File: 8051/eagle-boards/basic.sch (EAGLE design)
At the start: 29 parts, among them IC1 AT89S51-24P, IC2 ULN2003AN, IC3 ULN2003AN, Q1 12M

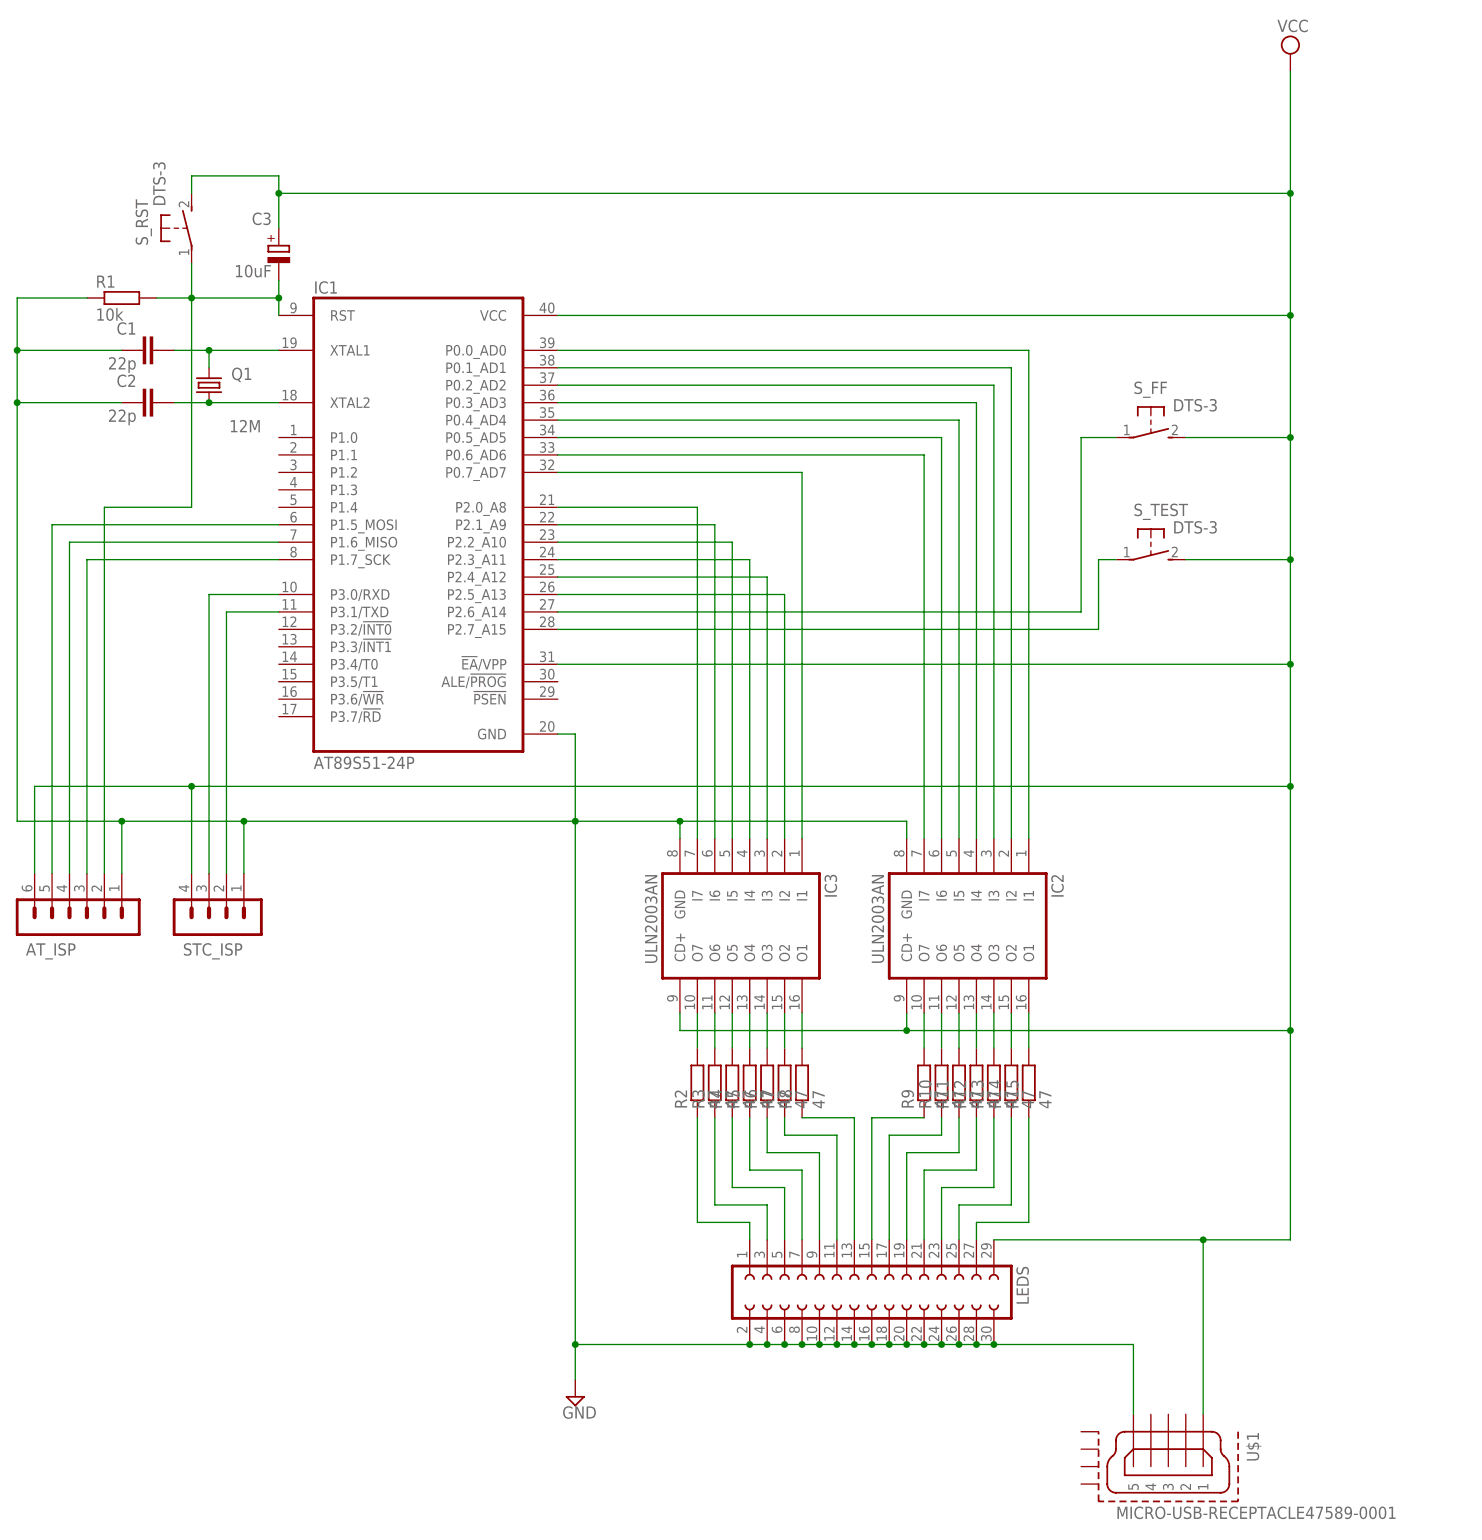
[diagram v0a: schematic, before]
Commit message: Split the actuation into its own board.
Note that the previous design was broken, as the Darlingtons weren't being grounded, but rather joined to Vcc.
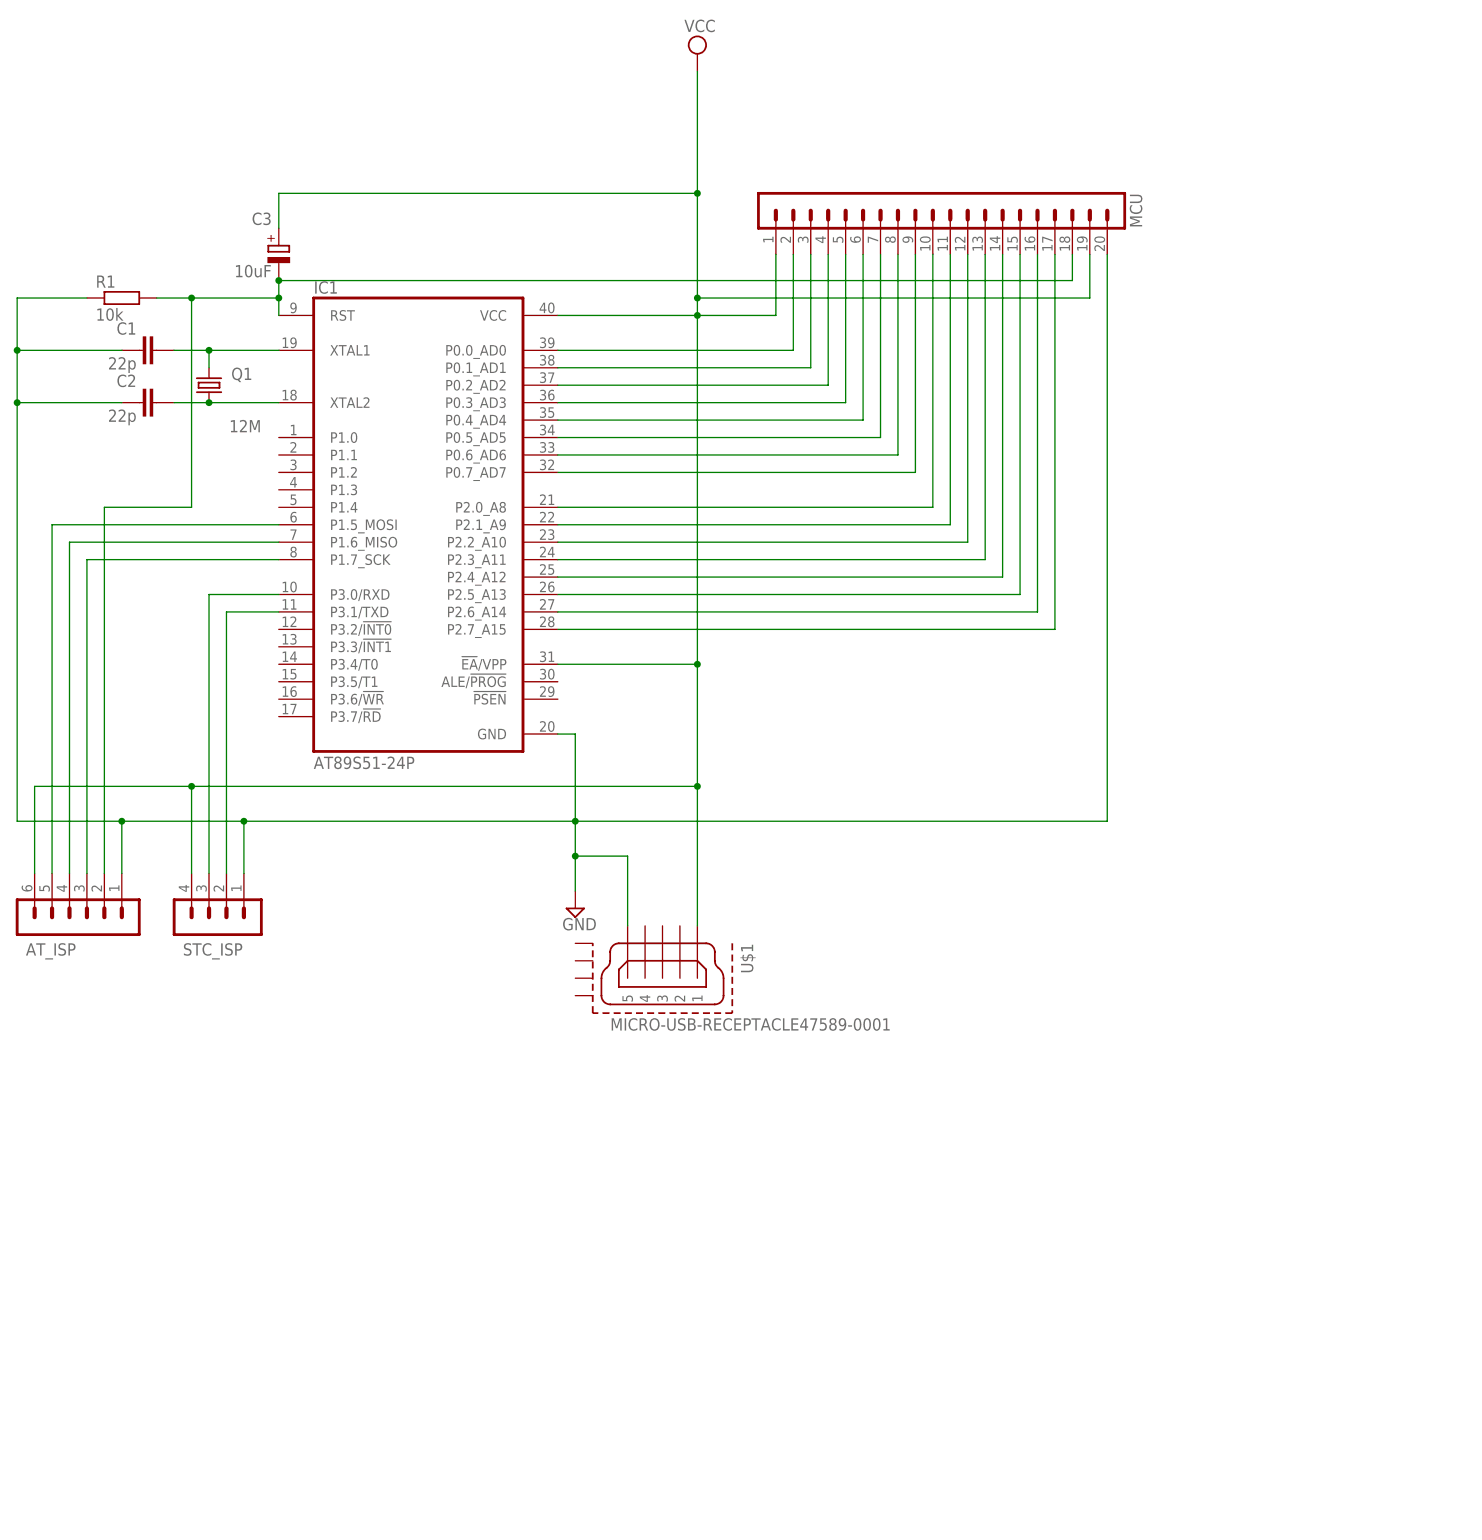
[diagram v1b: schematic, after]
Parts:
- removed IC2, IC3: ULN2003AN, uln-udn:ULN2003AN
- removed LEDS: (no value), con-lsta:FE15-2
- removed R10, R11, R12, R13, R14, R15, R2, R3, R4, R5, R6, R7, R8, R9: 47, rcl:R-EU_0207/10
- removed S_FF, S_RST, S_TEST: DTS-3, switch-tact:DTS-3
- added MCU: (no value), con-lstb:MA20-1
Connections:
- removed net N$21: IC3.O6, R3.2
- removed net N$22: IC3.O5, R4.2
- removed net N$23: IC3.O4, R5.2
- removed net N$24: IC3.O3, R6.2
- removed net N$25: IC3.O2, R7.2
- removed net N$26: IC3.O1, R8.2
- removed net N$27: IC2.O7, R9.2
- removed net N$28: IC2.O6, R10.2
- removed net N$29: IC2.O5, R11.2
- removed net N$30: IC2.O4, R12.2
- removed net N$31: IC2.O3, R13.2
- removed net N$32: IC2.O2, R14.2
- removed net N$33: IC2.O1, R15.2
- removed net N$34: LEDS.27, R15.1
- removed net N$35: LEDS.25, R14.1
- removed net N$36: LEDS.23, R13.1
- removed net N$37: LEDS.21, R12.1
- removed net N$38: LEDS.19, R11.1
- removed net N$39: LEDS.17, R10.1
- removed net N$40: LEDS.15, R9.1
- removed net N$41: LEDS.13, R8.1
- removed net N$42: LEDS.11, R7.1
- removed net N$43: LEDS.9, R6.1
- removed net N$44: LEDS.7, R5.1
- removed net N$45: LEDS.5, R4.1
- removed net N$46: LEDS.3, R3.1
- removed net N$47: LEDS.1, R2.1
- removed net N$48: IC1.P2.7_A15, S_TEST.1
- net GND: now also MCU.20; no longer IC2.GND, IC3.GND, LEDS.10, LEDS.12, LEDS.14, LEDS.16, LEDS.18, LEDS.2, LEDS.20, LEDS.22, LEDS.24, LEDS.26, LEDS.28, LEDS.30, LEDS.4, LEDS.6, LEDS.8
- net N$1: now also IC1.P0.0_AD0, MCU.2; no longer IC1.P2.0_A8, IC3.I7
- net N$10: now also IC1.P0.6_AD6, MCU.8; no longer IC1.P0.4_AD4, IC2.I5
- net N$11: now also IC1.P0.7_AD7, MCU.9; no longer IC1.P0.5_AD5, IC2.I6
- net N$12: now also IC1.P2.0_A8, MCU.10; no longer IC1.P0.6_AD6, IC2.I7
- net N$13: now also IC1.P2.1_A9, MCU.11; no longer IC1.P0.7_AD7, IC3.I1
- net N$14: now also MCU.12; no longer IC3.I5
- net N$15: now also MCU.13; no longer IC3.I4
- net N$16: now also MCU.14; no longer IC3.I3
- net N$17: now also MCU.15; no longer IC3.I2
- net N$19: now also MCU.16; no longer S_FF.1
- net N$2: now also IC1.P0.1_AD1, MCU.3; no longer IC1.P2.1_A9, IC3.I6
- net N$20: now also IC1.P2.7_A15, MCU.17; no longer IC3.O7, R2.2
- net N$5: now also MCU.18; no longer S_RST.1
- net N$6: now also IC1.P0.2_AD2, MCU.4; no longer IC1.P0.0_AD0, IC2.I1
- net N$7: now also IC1.P0.3_AD3, MCU.5; no longer IC1.P0.1_AD1, IC2.I2
- net N$8: now also IC1.P0.4_AD4, MCU.6; no longer IC1.P0.2_AD2, IC2.I3
- net N$9: now also IC1.P0.5_AD5, MCU.7; no longer IC1.P0.3_AD3, IC2.I4
- net VCC: now also MCU.1, MCU.19; no longer IC2.CD+, IC3.CD+, LEDS.29, S_FF.2, S_RST.2, S_TEST.2
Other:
- moved on the sheet: U$1

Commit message: Fix significant mistakes in the controller board.
The capacitors to stabilise the crystal need to be a bit beefier, make space for them.

Replace the pin header with a female header for the connection to the actuator board.

Necessary: add a resistor network between P0 and the connector.

P0 is the only port needing pull-up resistors.
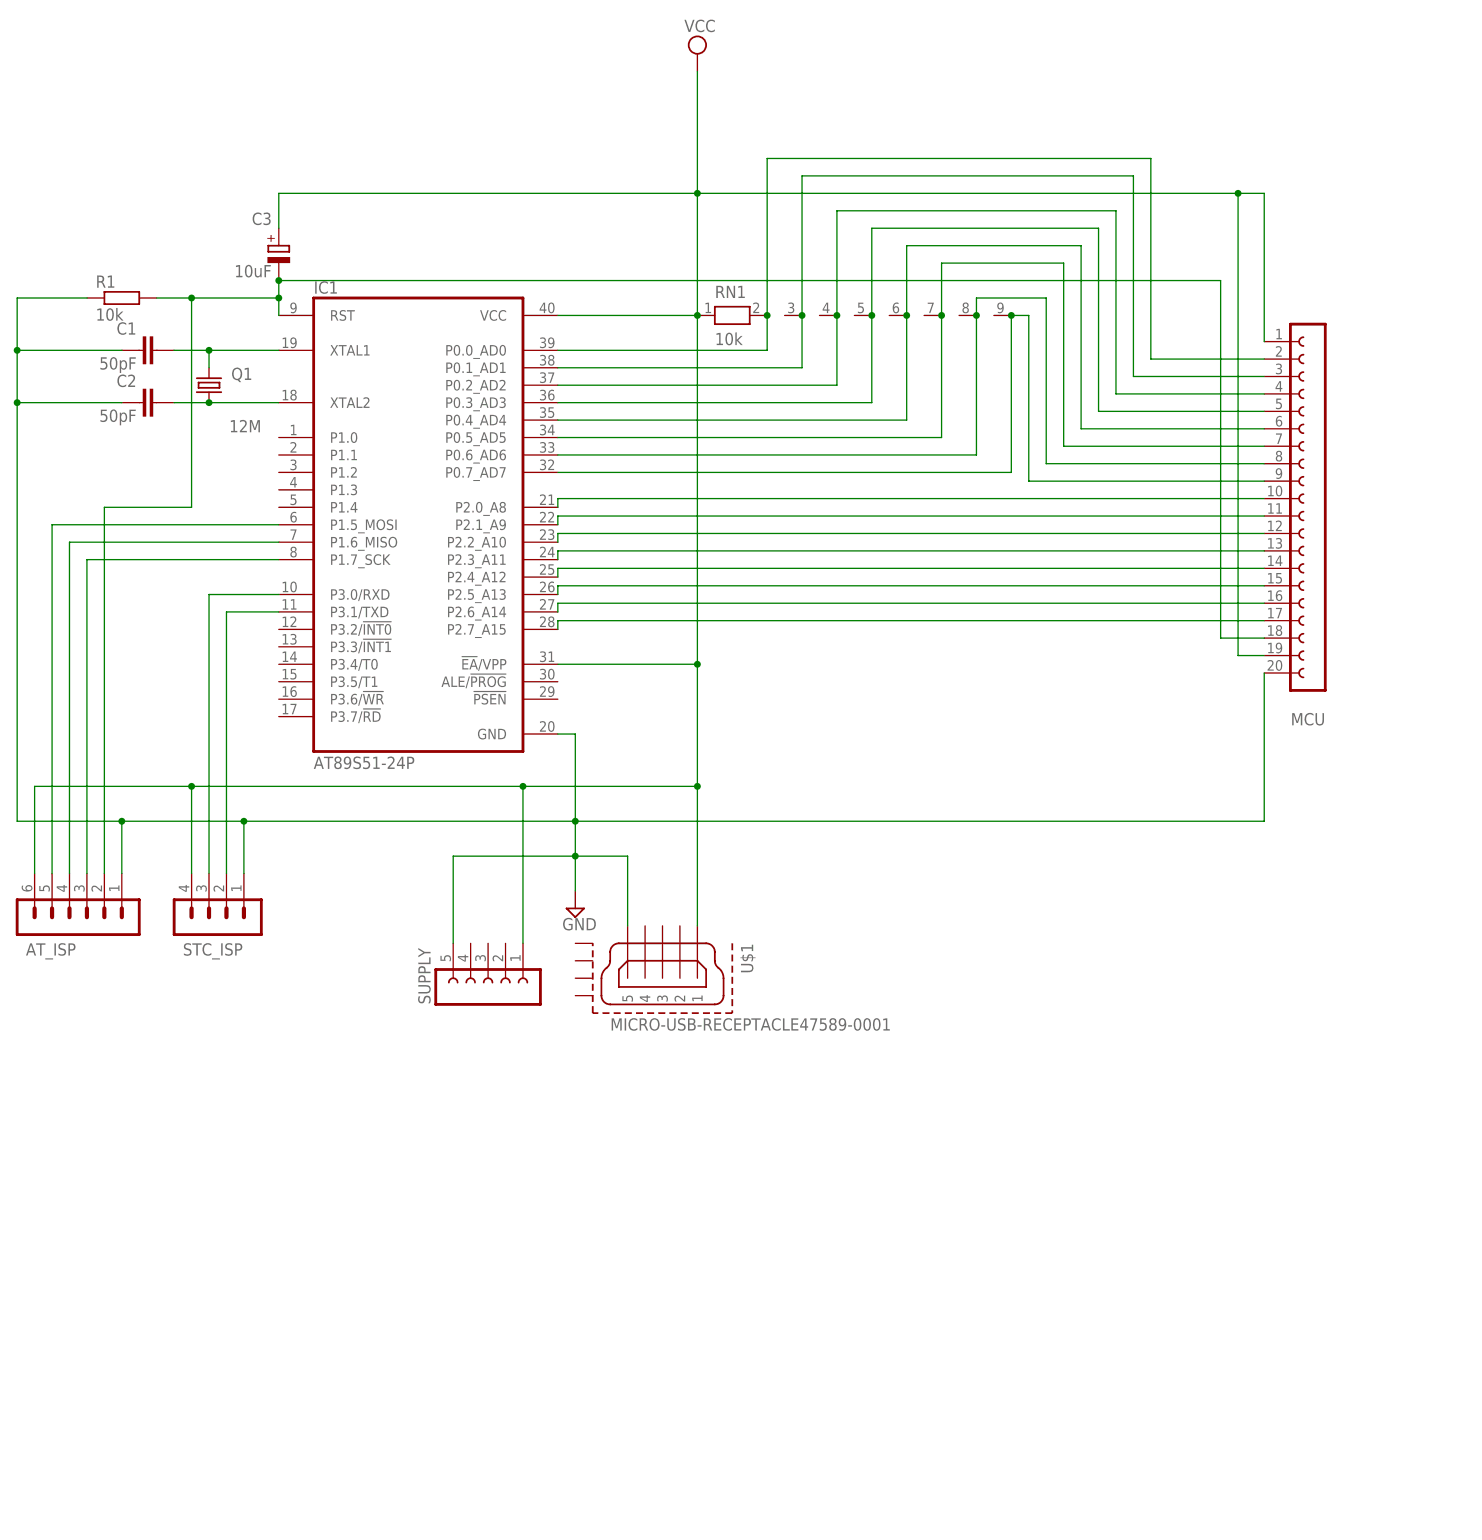
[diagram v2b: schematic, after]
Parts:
- added RN1: 10k, resistor-net:RN08
- added SUPPLY: (no value), con-lsta:FE05-1
- C1, C2: value 22p -> 50pF; device rcl:C-EU025-025X050 -> rcl:C-EU050-025X075
- MCU: device con-lstb:MA20-1 -> con-lsta:FE20-1
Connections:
- removed net N$1: IC1.P0.0_AD0, MCU.2
- removed net N$2 (its old number): IC1.P0.1_AD1, MCU.3
- removed net N$6 (its old number): IC1.P0.2_AD2, MCU.4
- removed net N$8 (its old number): IC1.P0.4_AD4, MCU.6
- removed net N$9 (its old number): IC1.P0.5_AD5, MCU.7
- new net N$12: IC1.P0.5_AD5, MCU.7, RN1.7
- new net N$13: IC1.P0.6_AD6, MCU.8, RN1.8
- new net N$14: IC1.P0.7_AD7, MCU.9, RN1.9
- new net N$22: IC1.P0.2_AD2, MCU.4, RN1.4
- new net N$26: IC1.P0.0_AD0, MCU.2, RN1.2
- net GND: now also SUPPLY.5
- net N$10: now also IC1.P0.3_AD3, MCU.5, RN1.5; no longer IC1.P0.6_AD6, MCU.8
- net N$11: now also IC1.P0.4_AD4, MCU.6, RN1.6; no longer IC1.P0.7_AD7, MCU.9
- net N$7: now also IC1.P0.1_AD1, MCU.3, RN1.3; no longer IC1.P0.3_AD3, MCU.5
- net VCC: now also RN1.1, SUPPLY.1
